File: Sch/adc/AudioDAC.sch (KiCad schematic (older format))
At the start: 26 parts, among them CN3 AudioJack, U6 NAU8822LYG, U7 TLV702

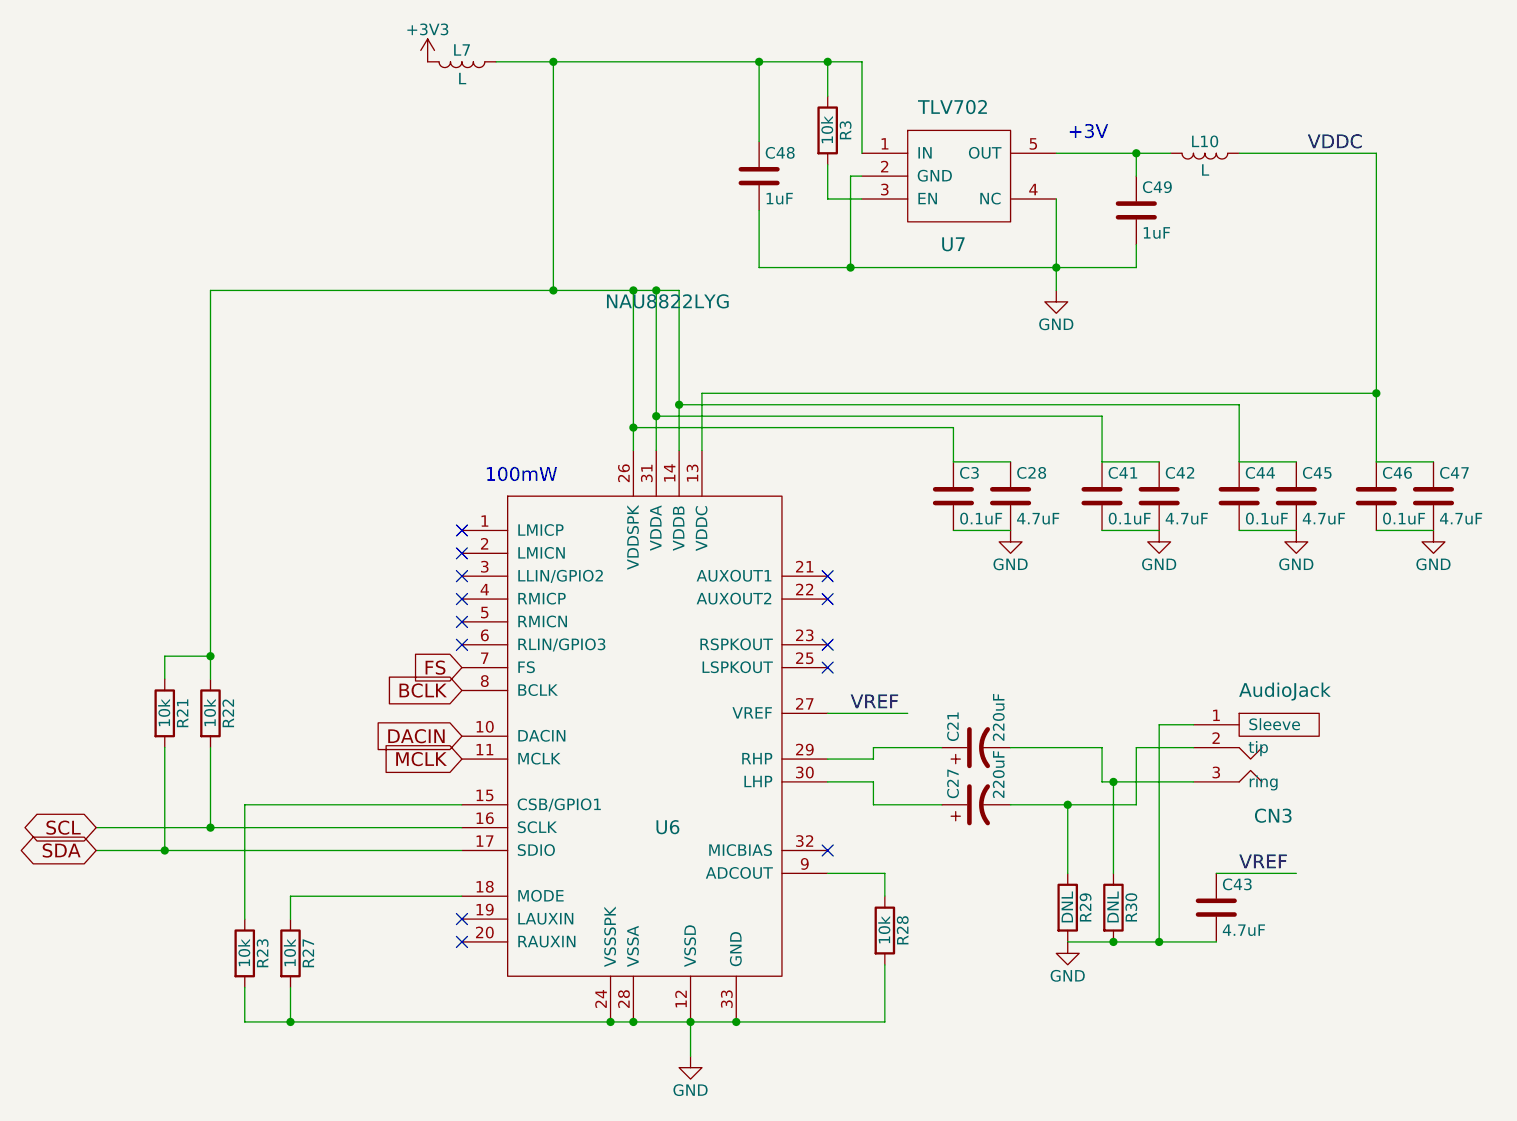
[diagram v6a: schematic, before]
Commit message: Analog front end is removed from the ADC board. ADC board is done
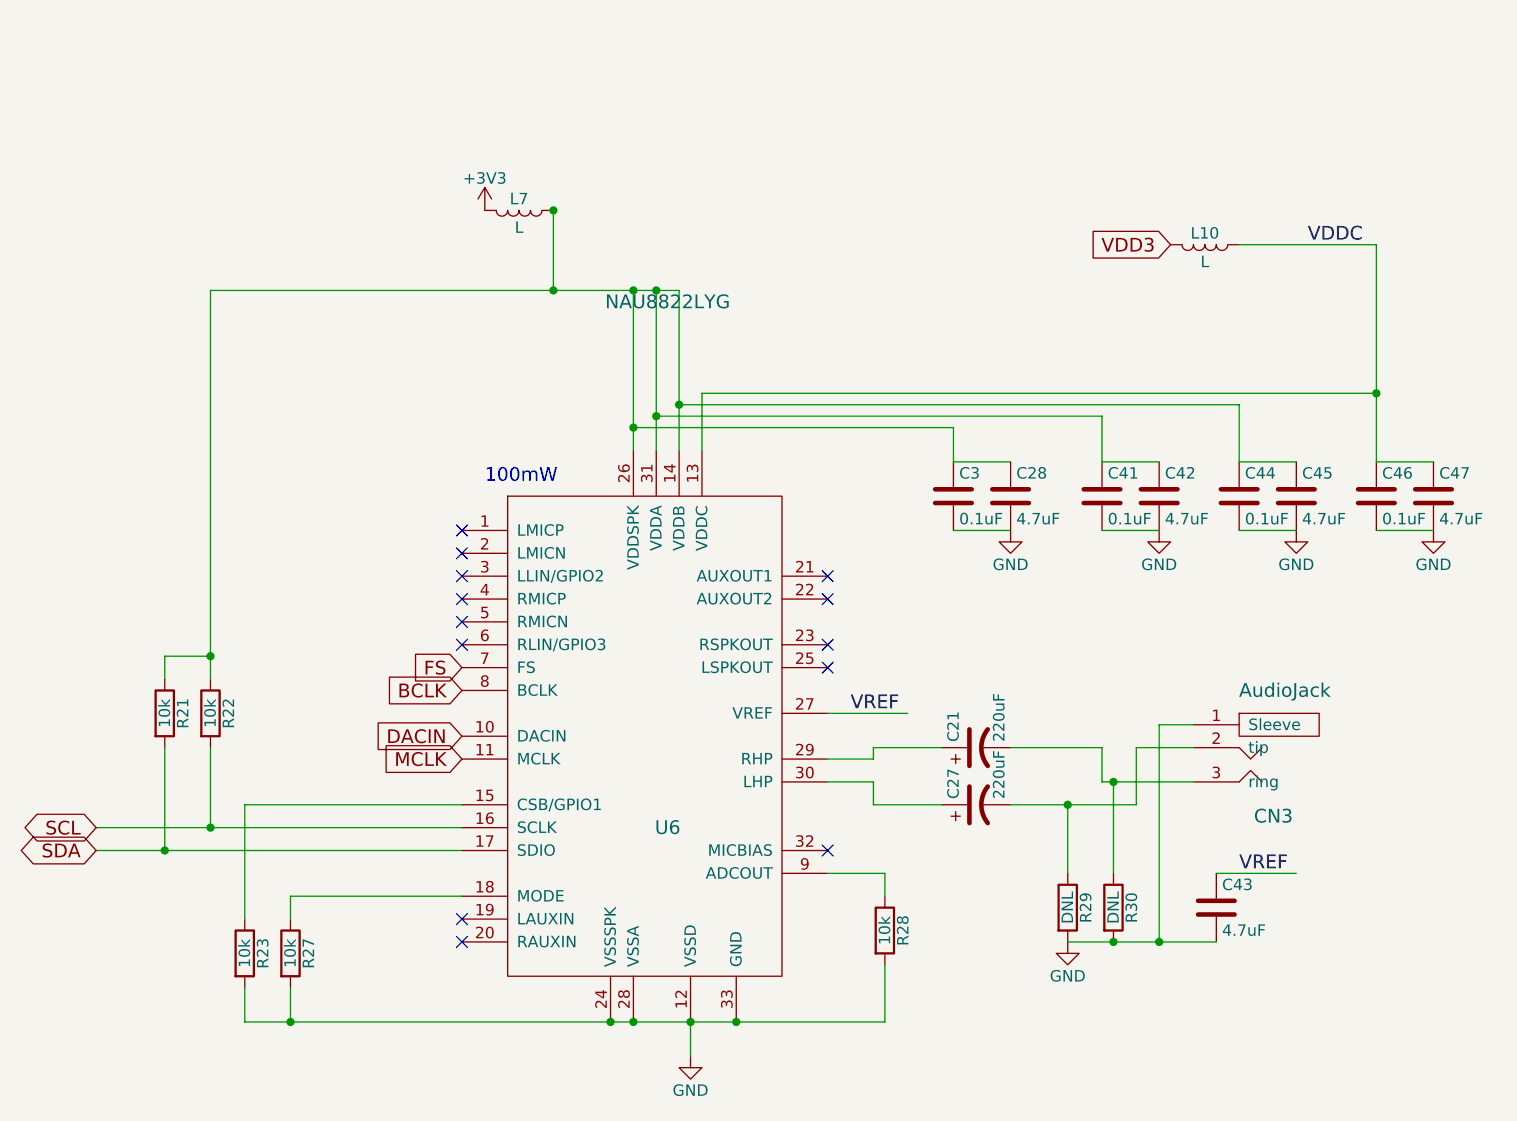
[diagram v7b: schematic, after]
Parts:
- removed C48, C49: 1uF, adc_lib:C0603, symbol C
- removed R3: 10k, adc_lib:R0603, symbol R
- removed U7: TLV702, adc_lib:TLV702, symbol TLV702
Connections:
- net labels added: VDD3
- wire segments 74 -> 60
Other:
- note removed: "+3V"
- moved on the sheet: L10, L7
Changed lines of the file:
@@
 $EndComp
 $Comp
-L GND #PWR053
+L GND #PWR049
 U 1 1 58A94BF7
 P 7300 4600
-F 0 "#PWR053" H 7300 4350 50  0001 C CNN
+F 0 "#PWR049" H 7300 4350 50  0001 C CNN
 F 1 "GND" H 7300 4450 50  0000 C CNN
 F 2 "" H 7300 4600 50  0000 C CNN
@@
 $EndComp
 $Comp
-L GND #PWR054
+L GND #PWR050
 U 1 1 58A96033
 P 5650 5100
-F 0 "#PWR054" H 5650 4850 50  0001 C CNN
+F 0 "#PWR050" H 5650 4850 50  0001 C CNN
 F 1 "GND" H 5650 4950 50  0000 C CNN
 F 2 "" H 5650 5100 50  0000 C CNN
@@
 $EndComp
 $Comp
-L GND #PWR056
+L GND #PWR051
 U 1 1 58A98E4C
 P 7050 2800
-F 0 "#PWR056" H 7050 2550 50  0001 C CNN
+F 0 "#PWR051" H 7050 2550 50  0001 C CNN
 F 1 "GND" H 7050 2650 50  0000 C CNN
 F 2 "" H 7050 2800 50  0000 C CNN
@@
 $EndComp
 $Comp
-L GND #PWR057
+L GND #PWR052
 U 1 1 58A99758
 P 7700 2800
-F 0 "#PWR057" H 7700 2550 50  0001 C CNN
+F 0 "#PWR052" H 7700 2550 50  0001 C CNN
 F 1 "GND" H 7700 2650 50  0000 C CNN
 F 2 "" H 7700 2800 50  0000 C CNN
@@
 $EndComp
 $Comp
-L GND #PWR058
+L GND #PWR053
 U 1 1 58A997A8
 P 8300 2800
-F 0 "#PWR058" H 8300 2550 50  0001 C CNN
+F 0 "#PWR053" H 8300 2550 50  0001 C CNN
 F 1 "GND" H 8300 2650 50  0000 C CNN
 F 2 "" H 8300 2800 50  0000 C CNN
@@
 $EndComp
 $Comp
-L GND #PWR059
+L GND #PWR054
 U 1 1 58A99804
 P 8900 2800
-F 0 "#PWR059" H 8900 2550 50  0001 C CNN
+F 0 "#PWR054" H 8900 2550 50  0001 C CNN
 F 1 "GND" H 8900 2650 50  0000 C CNN
 F 2 "" H 8900 2800 50  0000 C CNN
@@
 100mW
 $Comp
-L TLV702 U7
-U 1 1 58B42AD2
-P 6800 1250
-F 0 "U7" H 6800 950 60  0000 C CNN
-F 1 "TLV702" H 6800 1550 60  0000 C CNN
-F 2 "adc_lib:TLV702" H 6800 950 60  0001 C CNN
-F 3 "" H 6800 950 60  0001 C CNN
-	1    6800 1250
-	1    0    0    -1
-$EndComp
-$Comp
-L +3V3 #PWR060
+L +3V3 #PWR055
 U 1 1 58B42B1D
-P 4500 750
-F 0 "#PWR060" H 4500 600 50  0001 C CNN
-F 1 "+3V3" H 4500 890 50  0000 C CNN
-F 2 "" H 4500 750 50  0000 C CNN
-F 3 "" H 4500 750 50  0000 C CNN
-	1    4500 750
+P 4750 1400
+F 0 "#PWR055" H 4750 1250 50  0001 C CNN
+F 1 "+3V3" H 4750 1540 50  0000 C CNN
+F 2 "" H 4750 1400 50  0000 C CNN
+F 3 "" H 4750 1400 50  0000 C CNN
+	1    4750 1400
 	1    0    0    -1
 $EndComp
@@
 L L L7
 U 1 1 58B42B5D
-P 4650 750
-F 0 "L7" V 4600 750 50  0000 C CNN
-F 1 "L" V 4725 750 50  0000 C CNN
-F 2 "adc_lib:FB0805" H 4650 750 50  0001 C CNN
-F 3 "" H 4650 750 50  0000 C CNN
-	1    4650 750
+P 4900 1400
+F 0 "L7" V 4850 1400 50  0000 C CNN
+F 1 "L" V 4975 1400 50  0000 C CNN
+F 2 "adc_lib:FB0805" H 4900 1400 50  0001 C CNN
+F 3 "" H 4900 1400 50  0000 C CNN
+	1    4900 1400
 	0    1    1    0
-$EndComp
-$Comp
-L C C48
-U 1 1 58B42C50
-P 5950 1250
-F 0 "C48" H 5975 1350 50  0000 L CNN
-F 1 "1uF" H 5975 1150 50  0000 L CNN
-F 2 "adc_lib:C0603" H 5988 1100 50  0001 C CNN
-F 3 "" H 5950 1250 50  0000 C CNN
-	1    5950 1250
-	1    0    0    -1
-$EndComp
-$Comp
-L R R3
-U 1 1 58B42CBF
-P 6250 1050
-F 0 "R3" V 6330 1050 50  0000 C CNN
-F 1 "10k" V 6250 1050 50  0000 C CNN
-F 2 "adc_lib:R0603" V 6180 1050 50  0001 C CNN
-F 3 "" H 6250 1050 50  0000 C CNN
-	1    6250 1050
-	1    0    0    -1
-$EndComp
-$Comp
-L GND #PWR061
-U 1 1 58B42E0C
-P 7250 1750
-F 0 "#PWR061" H 7250 1500 50  0001 C CNN
-F 1 "GND" H 7250 1600 50  0000 C CNN
-F 2 "" H 7250 1750 50  0000 C CNN
-F 3 "" H 7250 1750 50  0000 C CNN
-	1    7250 1750
-	1    0    0    -1
-$EndComp
-$Comp
-L C C49
-U 1 1 58B42FBD
-P 7600 1400
-F 0 "C49" H 7625 1500 50  0000 L CNN
-F 1 "1uF" H 7625 1300 50  0000 L CNN
-F 2 "adc_lib:C0603" H 7638 1250 50  0001 C CNN
-F 3 "" H 7600 1400 50  0000 C CNN
-	1    7600 1400
-	1    0    0    -1
 $EndComp
 $Comp
 L L L10
 U 1 1 58B43AAD
-P 7900 1150
-F 0 "L10" V 7850 1150 50  0000 C CNN
-F 1 "L" V 7975 1150 50  0000 C CNN
-F 2 "adc_lib:FB0805" H 7900 1150 50  0001 C CNN
-F 3 "" H 7900 1150 50  0000 C CNN
-	1    7900 1150
+P 7900 1550
+F 0 "L10" V 7850 1550 50  0000 C CNN
+F 1 "L" V 7975 1550 50  0000 C CNN
+F 2 "adc_lib:FB0805" H 7900 1550 50  0001 C CNN
+F 3 "" H 7900 1550 50  0000 C CNN
+	1    7900 1550
 	0    1    1    0
 $EndComp
-Text Label 8350 1150 0    60   ~ 0
+Text Label 8350 1550 0    60   ~ 0
 VDDC
-Text Notes 7300 1100 0    60   ~ 0
-+3V
 Wire Wire Line
 	6250 3800 6450 3800
@@
 	8650 2500 8900 2500
 Wire Wire Line
-	8650 1150 8650 2500
+	8650 1550 8650 2500
 Wire Wire Line
 	5600 2250 8050 2250
@@
 Connection ~ 7300 4000
 Wire Wire Line
-	4800 750  6400 750
-Wire Wire Line
-	6250 1350 6400 1350
-Wire Wire Line
-	5950 1650 7600 1650
-Connection ~ 7250 1650
-Wire Wire Line
-	7250 1350 7250 1750
-Wire Wire Line
-	7250 1150 7750 1150
-Wire Wire Line
-	6400 1250 6350 1250
-Wire Wire Line
-	6350 1250 6350 1650
-Connection ~ 6350 1650
-Wire Wire Line
-	6400 750  6400 1150
-Connection ~ 6250 750
-Wire Wire Line
-	7600 1150 7600 1250
-Wire Wire Line
-	7600 1650 7600 1550
-Connection ~ 7600 1150
-Wire Wire Line
-	8050 1150 8650 1150
-Wire Wire Line
-	5950 1400 5950 1650
-Wire Wire Line
-	5950 1100 5950 750
-Wire Wire Line
-	6250 750  6250 900
-Wire Wire Line
-	6250 1350 6250 1200
+	8050 1550 8650 1550
 Connection ~ 5850 4950
-Connection ~ 5950 750
-Wire Wire Line
-	5050 1750 5050 750
-Connection ~ 5050 750
+Wire Wire Line
+	5050 1750 5050 1400
+Connection ~ 5050 1400
 Connection ~ 5050 1750
+Text GLabel 7750 1550 0    60   Input ~ 0
+VDD3
 $EndSCHEMATC
